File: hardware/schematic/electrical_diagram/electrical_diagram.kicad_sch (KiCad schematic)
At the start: 14 parts, among them Q1 NPN, U1 CAT24C256, U2 Display LCD ST7735, U3 LM293D

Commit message: hardware: fix haptic driver schematic, add title and authors
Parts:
- R4: value 1K -> 300-400
- R5: value 100K -> 47K-100K
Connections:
- net GND: now also D1.2 (A), Q1.3 (E); no longer Q1.1 (C)
- net Semnal PWM: now also A1.2 (GPIO1), R4.2
- new net: B1.N, Q1.1 (C)
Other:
- note added: "Beligan Tudor Filip Andrei-Robert Faculty of Automatic Control and Computer Engineering Iasi group 1309B"
- note added: "Dioda flyback"
- note added: "Driver Haptic handmade"
- note added: "GY-521"
- note added: "Motor haptic"
- note added: "Pedometer with a Tamagotchi-style video game interface and feedback audio-haptic."
- note added: "Protejeaza tranzistorul"
- note added: "Pull-down"
- note removed: "Additional pin functions: https://pinout.xyz/"
- note removed: "Intrebari:"
- note removed: "Sens dioda bun? Sens tranzistor bun? Valori rezistente bune?"
- moved on the sheet: D1, Q1

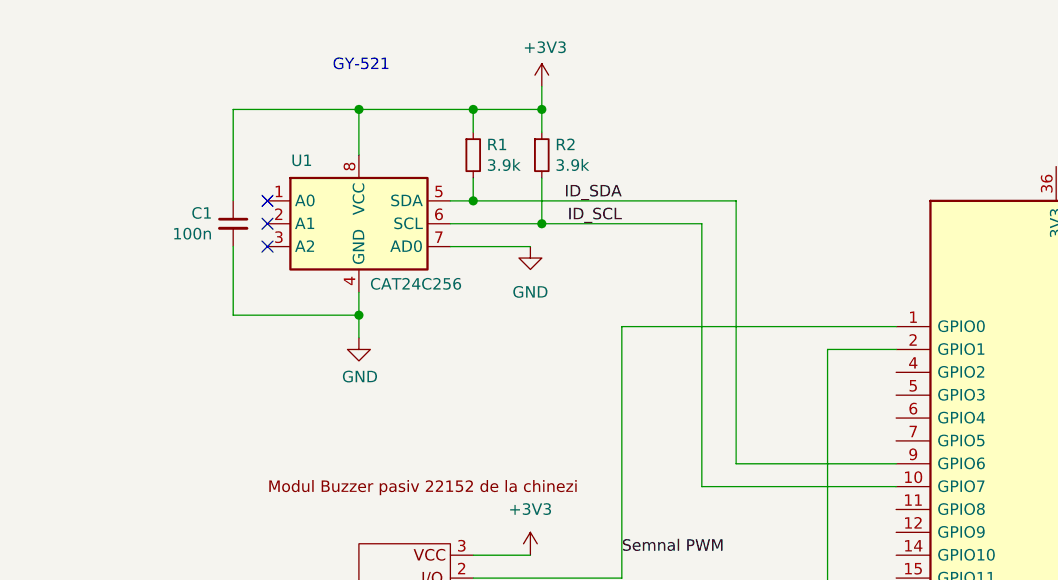
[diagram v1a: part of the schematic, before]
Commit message: hardware: update GYA INT pin on schematic
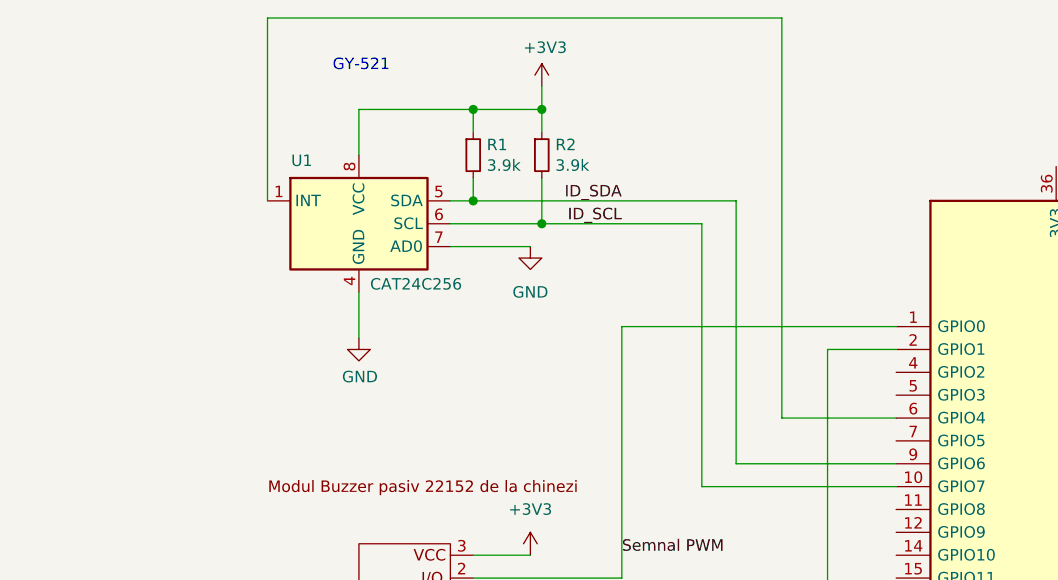
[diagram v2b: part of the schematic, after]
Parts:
- removed C1: 100n, symbol Device:C_Small
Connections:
- net at U1.1 (INT): now also A1.6 (GPIO4)
- no-connect marks 3 -> 0
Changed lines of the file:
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@@
-	)
-	(junction
-		(at 85.09 49.53)
-		(diameter 1.016)
-		(color 0 0 0 0)
-	)
-	(junction
-		(at 85.09 26.67)
-		(diameter 1.016)
-		(color 0 0 0 0)
 	)
 	(junction
@@
 		(color 0 0 0 0)
 	)
-	(no_connect
-		(at 74.93 36.83)
-	)
-	(no_connect
-		(at 74.93 39.37)
-	)
-	(no_connect
-		(at 74.93 41.91)
-	)
 	(wire
 		(pts
@@
 	(wire
 		(pts
+			(xy 74.93 36.83) (xy 74.93 16.51)
+		)
+		(stroke
+			(width 0)
+			(type default)
+		)
+	)
+	(wire
+		(pts
 			(xy 146.05 143.51) (xy 146.05 148.59)
 		)
@@
 	(wire
 		(pts
+			(xy 132.08 16.51) (xy 132.08 60.96)
+		)
+		(stroke
+			(width 0)
+			(type default)
+		)
+	)
+	(wire
+		(pts
 			(xy 231.14 35.56) (xy 243.84 35.56)
 		)
@@
 	(wire
 		(pts
+			(xy 74.93 16.51) (xy 132.08 16.51)
+		)
+		(stroke
+			(width 0)
+			(type default)
+		)
+	)
+	(wire
+		(pts
 			(xy 190.5 58.42) (xy 198.12 58.42)
 		)
@@
 	(wire
 		(pts
+			(xy 132.08 60.96) (xy 144.78 60.96)
+		)
+		(stroke
+			(width 0)
+			(type default)
+		)
+	)
+	(wire
+		(pts
 			(xy 133.35 88.9) (xy 133.35 120.65)
 		)
@@
 	(wire
 		(pts
-			(xy 71.12 26.67) (xy 71.12 36.83)
-		)
-		(stroke
-			(width 0)
-			(type solid)
-		)
-	)
-	(wire
-		(pts
-			(xy 71.12 41.91) (xy 71.12 49.53)
-		)
-		(stroke
-			(width 0)
-			(type solid)
-		)
-	)
-	(wire
-		(pts
-			(xy 71.12 49.53) (xy 85.09 49.53)
-		)
-		(stroke
-			(width 0)
-			(type solid)
-		)
-	)
-	(wire
-		(pts
-			(xy 85.09 26.67) (xy 71.12 26.67)
-		)
-		(stroke
-			(width 0)
-			(type solid)
-		)
-	)
-	(wire
-		(pts
-			(xy 85.09 46.99) (xy 85.09 49.53)
-		)
-		(stroke
-			(width 0)
-			(type solid)
-		)
-	)
-	(wire
-		(pts
-			(xy 85.09 49.53) (xy 85.09 52.07)
+			(xy 85.09 46.99) (xy 85.09 52.07)
 		)
 		(stroke
@@
 			)
 			(justify right bottom)
-		)
-	)
-	(symbol
-		(lib_id "Device:C_Small")
-		(at 71.12 39.37 0)
-		(unit 1)
-		(body_style 1)
-		(exclude_from_sim no)
-		(in_bom yes)
-		(on_board yes)
-		(in_pos_files yes)
-		(dnp no)
-		(property "Reference" "C1"
-			(at 68.7958 38.2206 0)
-			(show_name no)
-			(do_not_autoplace no)
-			(effects
-				(font
-					(size 1.27 1.27)
-				)
-				(justify right)
-			)
-		)
-		(property "Value" "100n"
-			(at 68.7958 40.5193 0)
-			(show_name no)
-			(do_not_autoplace no)
-			(effects
-				(font
-					(size 1.27 1.27)
-				)
-				(justify right)
-			)
-		)
-		(property "Footprint" ""
-			(at 71.12 39.37 0)
-			(hide yes)
-			(show_name no)
-			(do_not_autoplace no)
-			(effects
-				(font
-					(size 1.27 1.27)
-				)
-			)
-		)
-		(property "Datasheet" ""
-			(at 71.12 39.37 0)
-			(hide yes)
-			(show_name no)
-			(do_not_autoplace no)
-			(effects
-				(font
-					(size 1.27 1.27)
-				)
-			)
-		)
-		(property "Description" "Unpolarized capacitor, small symbol"
-			(at 71.12 39.37 0)
-			(hide yes)
-			(show_name no)
-			(do_not_autoplace no)
-			(effects
-				(font
-					(size 1.27 1.27)
-				)
-			)
-		)
-		(pin "1"
-		)
-		(pin "2"
-		)
-		(instances
-			(project "electrical_diagram"
-				(path "/e63e39d7-6ac0-4ffd-8aa3-1841a4541b55"
-					(reference "C1")
-					(unit 1)
-				)
-			)
 		)
 	)
@@
 		(pin "1"
 		)
-		(pin "2"
-		)
-		(pin "3"
-		)
 		(pin "4"

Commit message: feat: Some drawing logic
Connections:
- net +3V3: now also D1.2 (A); no longer D1.1 (K)
- net GND: now also D1.1 (K); no longer D1.2 (A)
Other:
- moved on the sheet: D1
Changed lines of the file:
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@@
 	(text "Driver Haptic handmade"
 		(exclude_from_sim no)
-		(at 70.612 121.666 0)
+		(at 68.58 117.856 0)
 		(effects
 			(font
@@
 	(text "Dioda flyback"
 		(exclude_from_sim no)
-		(at 61.214 127.508 0)
+		(at 51.562 125.476 0)
 		(effects
 			(font
@@
 	)
 	(junction
+		(at 64.77 130.81)
+		(diameter 0)
+		(color 0 0 0 0)
+	)
+	(junction
 		(at 91.44 142.24)
 		(diameter 0)
@@
 	)
 	(junction
-		(at 64.77 130.81)
-		(diameter 0)
-		(color 0 0 0 0)
-	)
-	(junction
 		(at 97.79 26.67)
 		(diameter 1.016)
@@
 	(wire
 		(pts
+			(xy 64.77 130.81) (xy 78.74 130.81)
+		)
+		(stroke
+			(width 0)
+			(type default)
+		)
+	)
+	(wire
+		(pts
 			(xy 232.41 71.12) (xy 232.41 46.99)
 		)
@@
 		(pts
 			(xy 231.14 35.56) (xy 243.84 35.56)
-		)
-		(stroke
-			(width 0)
-			(type default)
-		)
-	)
-	(wire
-		(pts
-			(xy 64.77 130.81) (xy 78.74 130.81)
 		)
 		(stroke
@@
 	(symbol
 		(lib_id "Diode:1N914")
-		(at 60.96 130.81 0)
+		(at 60.96 130.81 180)
 		(unit 1)
 		(body_style 1)
@@
 		(dnp no)
 		(property "Reference" "D1"
-			(at 60.706 137.414 0)
+			(at 61.214 124.206 0)
 			(show_name no)
 			(do_not_autoplace no)
@@
 		)
 		(property "Value" "1N914"
-			(at 59.436 134.874 0)
+			(at 62.484 126.746 0)
 			(show_name no)
 			(do_not_autoplace no)
@@
 		)
 		(property "Footprint" "Diode_THT:D_DO-35_SOD27_P7.62mm_Horizontal"
-			(at 60.96 135.255 0)
-			(hide yes)
-			(show_name no)
+			(at 60.96 126.365 0)
+			(hide yes)
+			(show_name no)

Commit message: niste unsaved changes
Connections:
- net Semnal PWM: now also A1.26 (GPIO20); no longer A1.2 (GPIO1)
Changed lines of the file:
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@@
-	(wire
-		(pts
-			(xy 137.16 81.28) (xy 137.16 53.34)
-		)
-		(stroke
-			(width 0)
-			(type default)
-		)
-	)
 	(wire
 		(pts
@@
 	(wire
 		(pts
+			(xy 115.57 142.24) (xy 115.57 129.54)
+		)
+		(stroke
+			(width 0)
+			(type default)
+		)
+	)
+	(wire
+		(pts
 			(xy 232.41 46.99) (xy 243.84 46.99)
 		)
@@
 	(wire
 		(pts
+			(xy 115.57 129.54) (xy 193.04 129.54)
+		)
+		(stroke
+			(width 0)
+			(type default)
+		)
+	)
+	(wire
+		(pts
 			(xy 231.14 35.56) (xy 243.84 35.56)
 		)
@@
 	(wire
 		(pts
-			(xy 115.57 81.28) (xy 137.16 81.28)
-		)
-		(stroke
-			(width 0)
-			(type default)
-		)
-	)
-	(wire
-		(pts
 			(xy 132.08 60.96) (xy 144.78 60.96)
 		)
@@
 	(wire
 		(pts
-			(xy 115.57 81.28) (xy 115.57 142.24)
-		)
-		(stroke
-			(width 0)
-			(type default)
-		)
-	)
-	(wire
-		(pts
 			(xy 198.12 58.42) (xy 198.12 146.05)
 		)
@@
 	(wire
 		(pts
-			(xy 137.16 53.34) (xy 144.78 53.34)
-		)
-		(stroke
-			(width 0)
-			(type default)
-		)
-	)
-	(wire
-		(pts
 			(xy 85.09 46.99) (xy 85.09 52.07)
 		)
@@
 	(wire
 		(pts
+			(xy 193.04 129.54) (xy 193.04 68.58)
+		)
+		(stroke
+			(width 0)
+			(type default)
+		)
+	)
+	(wire
+		(pts
 			(xy 133.35 120.65) (xy 214.63 120.65)
 		)
@@
 		)
 		(stroke
+			(width 0)
+			(type default)
+		)
+	)
+	(wire
+		(pts
+			(xy 193.04 68.58) (xy 190.5 68.58)
+		)
+		(stroke
